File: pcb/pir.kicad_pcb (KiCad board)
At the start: 2 copper layers, 80 x 100 mm, 137 parts, among them IC1 MAX44009EDT+T, IC2 IRA-S210ST01, IC3 EL817S, IC4 EL817S, IC7 EL817S, IC8 EL817S, J1 SJ-2523-SMT-TR, J2 FH12-24S-0.5SH(55), J3 SWD, J4 UART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

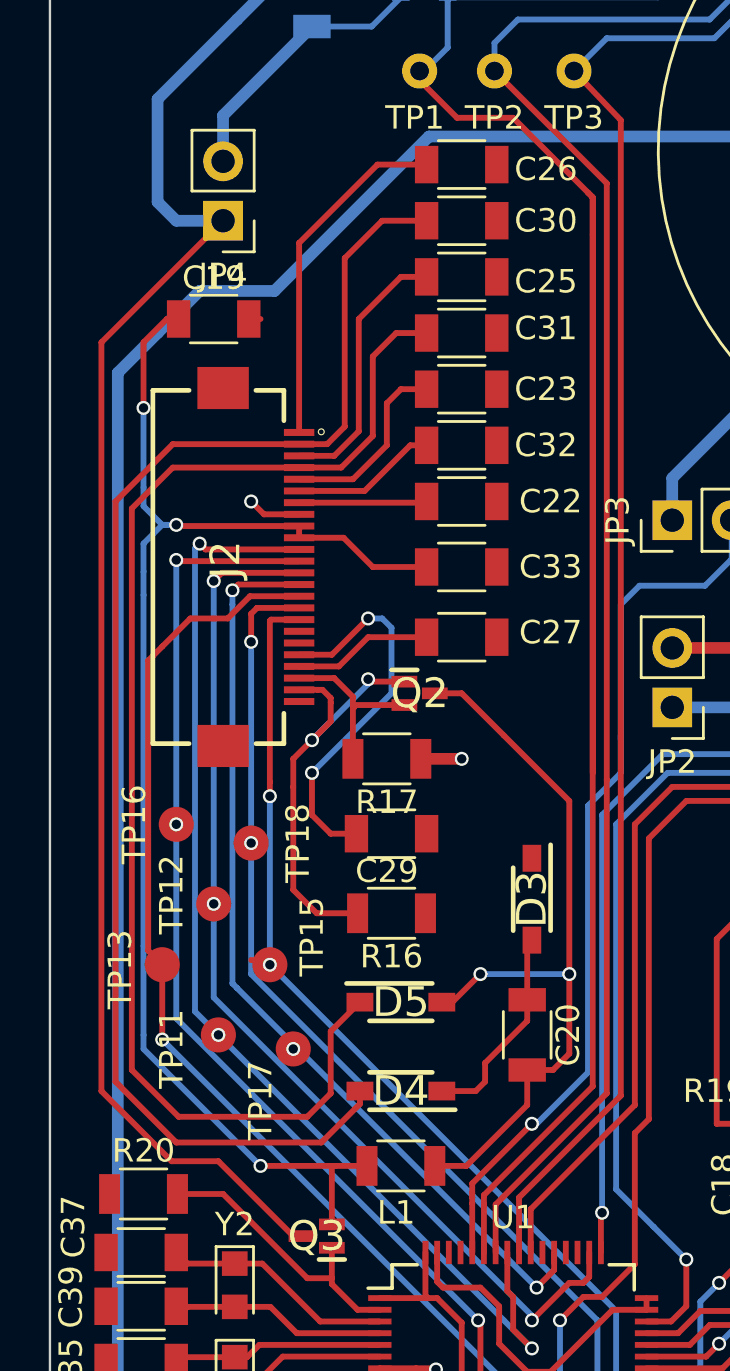
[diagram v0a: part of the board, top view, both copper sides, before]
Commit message: Changed FPC display connector
Same model from Hirose but Top-connect not Bottom-connect as it
previously was. Huge mistake, got it in time.

Created GDEW027W3 schematic symbol for the display.
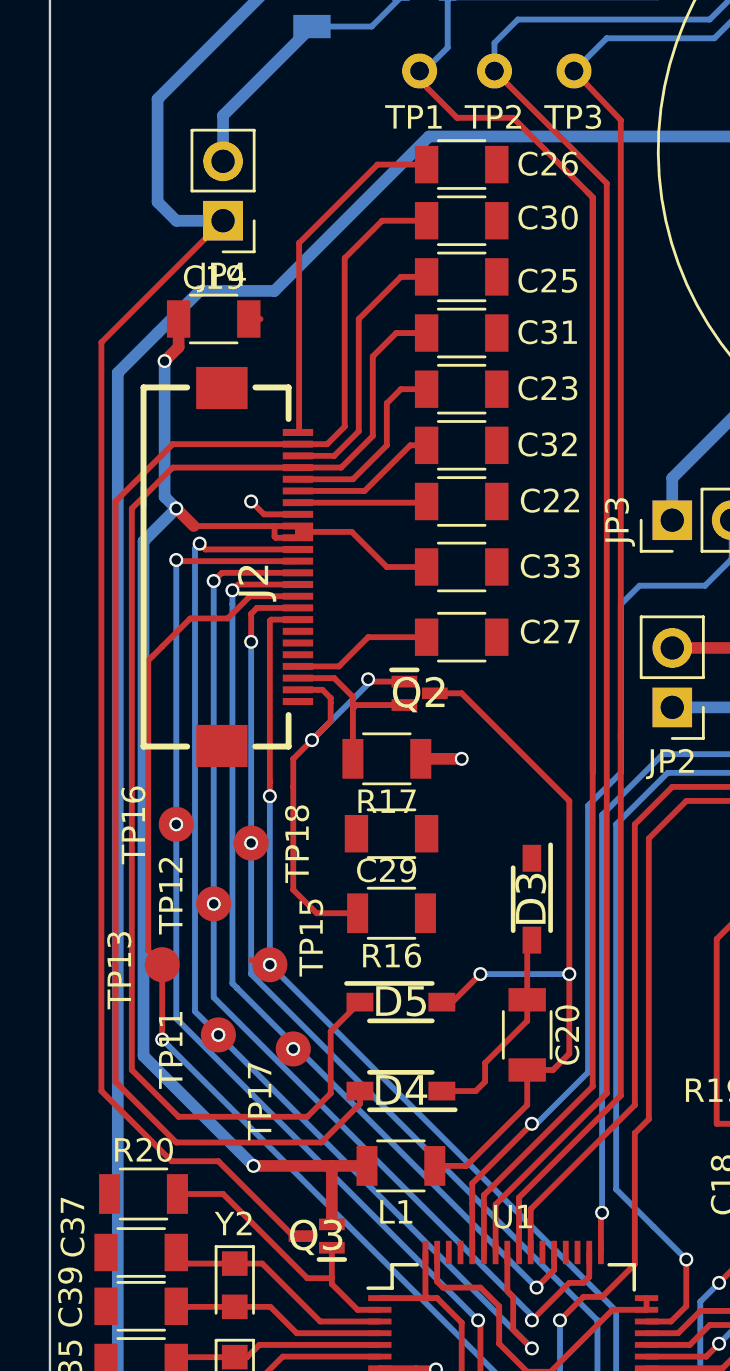
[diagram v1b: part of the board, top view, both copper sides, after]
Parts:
- J2: value FH12-24S-0.5SH(55) -> GDEW027W3; footprint FH12-24S-0.5SH(55):FH12-24S-0.5SH(55) -> FH12A-24S-0.5SH(55):FH12A-24S-0.5SH
- moved J2 0.20 mm to (53.4, 54.6), turned to 90 degrees
- turned C26 to 0 degrees
- turned C30 to 180 degrees
- turned C31 to 180 degrees
- turned C32 to 180 degrees
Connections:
- C26 pad 1: Earth -> Net-(C26-Pad1)
- C26 pad 2: Net-(C26-Pad2) -> Earth
- C30 pad 1: /user/PREVGL -> Earth
- C30 pad 2: Earth -> /user/PREVGL
- C31 pad 1: /user/PREVGH -> Earth
- C31 pad 2: Earth -> /user/PREVGH
- C32 pad 1: Net-(C32-Pad1) -> Earth
- C32 pad 2: Earth -> Net-(C32-Pad2)
- J2 pad 1: Net-(C26-Pad2) -> Net-(J2-Pad1)
- J2 pad 10: /user/EINK_VCC -> /soc/EINK_RST
- J2 pad 11: /soc/EINK_MOSI -> /soc/EINK_D/C
- J2 pad 12: /soc/EINK_SCK -> /soc/EINK_CS
- J2 pad 13: /soc/EINK_CS -> /soc/EINK_SCK
- J2 pad 14: /soc/EINK_D/C -> /soc/EINK_MOSI
- J2 pad 15: /soc/EINK_RST -> /user/EINK_VCC
- J2 pad 16: /soc/EINK_BUSY -> /user/EINK_VCC
- J2 pad 17: /soc/EINK_BS -> Earth
- J2 pad 18: Net-(J2-Pad18) -> Net-(C22-Pad2)
- J2 pad 19: Net-(J2-Pad19) -> Net-(C32-Pad2)
- J2 pad 2: /user/PREVGL -> /user/GDR
- J2 pad 20: Net-(C29-Pad1) -> Net-(C23-Pad2)
- J2 pad 21: Net-(C27-Pad2) -> /user/PREVGH
- J2 pad 22: /user/RESE -> Net-(C25-Pad2)
- J2 pad 23: /user/GDR -> /user/PREVGL
- J2 pad 24: Net-(J2-Pad24) -> Net-(C26-Pad1)
- J2 pad 3: Net-(C25-Pad2) -> /user/RESE
- J2 pad 4: /user/PREVGH -> Net-(C27-Pad2)
- J2 pad 5: Net-(C23-Pad2) -> Net-(J2-Pad5)
- J2 pad 6: Net-(C32-Pad1) -> Net-(J2-Pad6)
- J2 pad 7: Net-(C22-Pad2) -> Net-(J2-Pad7)
- J2 pad 8: Earth -> /soc/EINK_BS
- J2 pad 9: /user/EINK_VCC -> /soc/EINK_BUSY
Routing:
- net Net-(C29-Pad1): track 16.5 -> 0.07 mm, vias 2 -> 0
- net Net-(C26-Pad1): track 0.00 -> 15.0 mm
- net Net-(C26-Pad2): track 14.9 -> 0.00 mm
- net Net-(C32-Pad2): track 0.00 -> 6.26 mm
- net Net-(C32-Pad1): track 6.26 -> 0.00 mm
- net /user/EINK_VCC: track 60.0 -> 61.6 mm
- net (no net): track 0.00 -> 0.80 mm
